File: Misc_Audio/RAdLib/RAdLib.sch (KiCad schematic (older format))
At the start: 18 parts, among them U1 YM3812, U2 YM3014B, U3 RC4136

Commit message: Checkpoint ... board is close to being done.  Still need to tweak the ground plane.
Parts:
- added C1, C2, C3, C4: .1uF, Capacitor_THT:C_Disc_D5.0mm_W2.5mm_P2.50mm, symbol Device:C_Small
- added C5, C56, C6, C61, C7: 10uF, Capacitor_THT:CP_Radial_D5.0mm_P2.50mm, symbol Device:CP1
- added C57: 4.7uF, Capacitor_THT:CP_Radial_D5.0mm_P2.50mm, symbol Device:CP1
- added C58: 1000pF, Capacitor_THT:C_Disc_D5.0mm_W2.5mm_P2.50mm, symbol Device:C
- added C59: 270pF, Capacitor_THT:C_Disc_D5.0mm_W2.5mm_P2.50mm, symbol Device:C
- added C60: .1uF, Capacitor_THT:C_Disc_D5.0mm_W2.5mm_P2.50mm, symbol Device:C
- added C62: .047uF, Capacitor_THT:C_Disc_D5.0mm_W2.5mm_P2.50mm, symbol Device:C
- added C63: 220uF, Capacitor_THT:CP_Axial_L18.0mm_D8.0mm_P25.00mm_Horizontal, symbol Device:CP1
- added D1: 1N4148, Diode_THT:D_DO-35_SOD27_P7.62mm_Horizontal, symbol Device:D
- added J5: AudioJack3, jrt-Connectors:Jack_3.5mm_STX-3120-3B, symbol Connector:AudioJack3
- added Q1: 2N3904, Package_TO_SOT_THT:TO-92_HandSolder, symbol Transistor_BJT:2N3904
- added R10, R12: 2.2K, Resistor_THT:R_Axial_DIN0204_L3.6mm_D1.6mm_P5.08mm_Horizontal, symbol Device:R
- added R11, R15: 10K, Resistor_THT:R_Axial_DIN0204_L3.6mm_D1.6mm_P5.08mm_Horizontal, symbol Device:R
- added R13: 8.2K, Resistor_THT:R_Axial_DIN0204_L3.6mm_D1.6mm_P5.08mm_Horizontal, symbol Device:R
- added R14, R16, R17: 10R, Resistor_THT:R_Axial_DIN0204_L3.6mm_D1.6mm_P5.08mm_Horizontal, symbol Device:R
- added RV1: 10K, jrt-Potentiometers:Potentiometer_Bourns_91A1x_A24, symbol Device:R_POT
- added U4: LM386, Package_DIP:DIP-8_W7.62mm, symbol Amplifier_Audio:LM386
- renumbered C1 to C51, C2 to C52, C3 to C53, C4 to C54, C5 to C55
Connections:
- net FILTER_OUT: now also U3.12, C57.1; no longer U3.3
- net GND: now also C1.2, C2.2, C3.2, C4.2, C5.2, C58.2, C59.2, C6.2, C60.2, C61.2, C7.2, D1.2 (A), J5.S, Q1.1 (E), R11.2, R14.2, R15.2, RV1.3, U4.4 (GND)
- net VCC: now also C1.1, C2.1, C3.1, C4.1, C5.1, C56.1, C6.1, C7.1, U4.6 (V+)
- net at C51.1, U2.7 (RB): now also U3.2 (+); no longer U3.9 (+)
- net at C52.1, R3.1: now also U3.9 (+); no longer U3.2 (+)
- net at C53.1, R4.1, R6.2: now also U3.10; no longer U3.3
- net at R4.2, R5.2: now also U3.8 (-); no longer U3.1 (-)
- net at C54.1, R7.1: now also U3.13 (+); no longer U3.2 (+)
- net at R8.2, R9.2: now also U3.14 (-); no longer U3.1 (-)
- new net: U2.8 (MP), U3.1 (-), U3.3
- new net: C56.2, D1.1 (K), R10.2
- new net: Q1.2 (B), R10.1
- new net: C60.1, U4.2 (-)
- new net: C61.1, U4.7 (BYPASS)
- new net: C62.2, R14.1
- new net AMP_IN: RV1.2, U4.3 (+)
- new net AMP_OUT: C62.1, C63.1, U4.5
- new net AUDIO_OUT: C63.2, R15.1, R16.2, R17.2
- new net LEFT_OUT: J5.T, R16.1
- new net RC1: C57.2, Q1.3 (C), R11.1, R12.2
- new net RC2: C58.1, R12.1, R13.2
- new net RC3: C59.1, R13.1, RV1.1
- new net RIGHT_OUT: J5.R, R17.1
- no-connect marks 0 -> 2
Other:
- note added: "Audio taper"

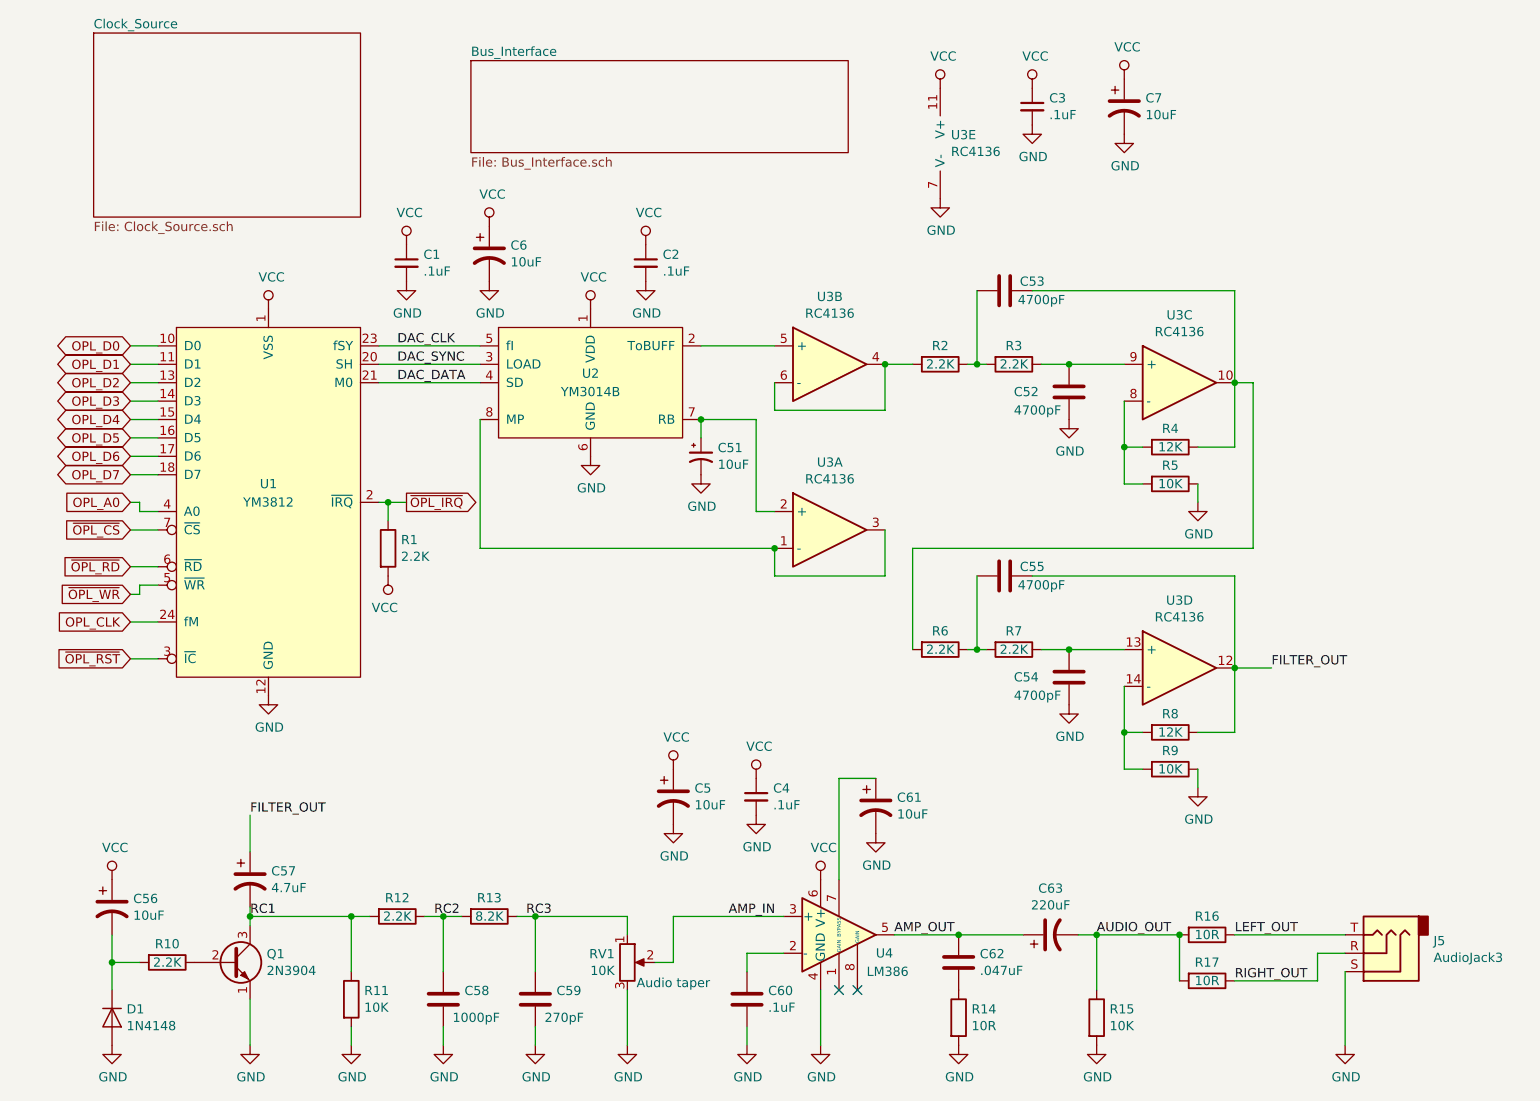
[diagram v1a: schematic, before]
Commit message: Rework the clock to use a self-contained oscillator package.  Remove dependencies on the 7404 in the bus interface.
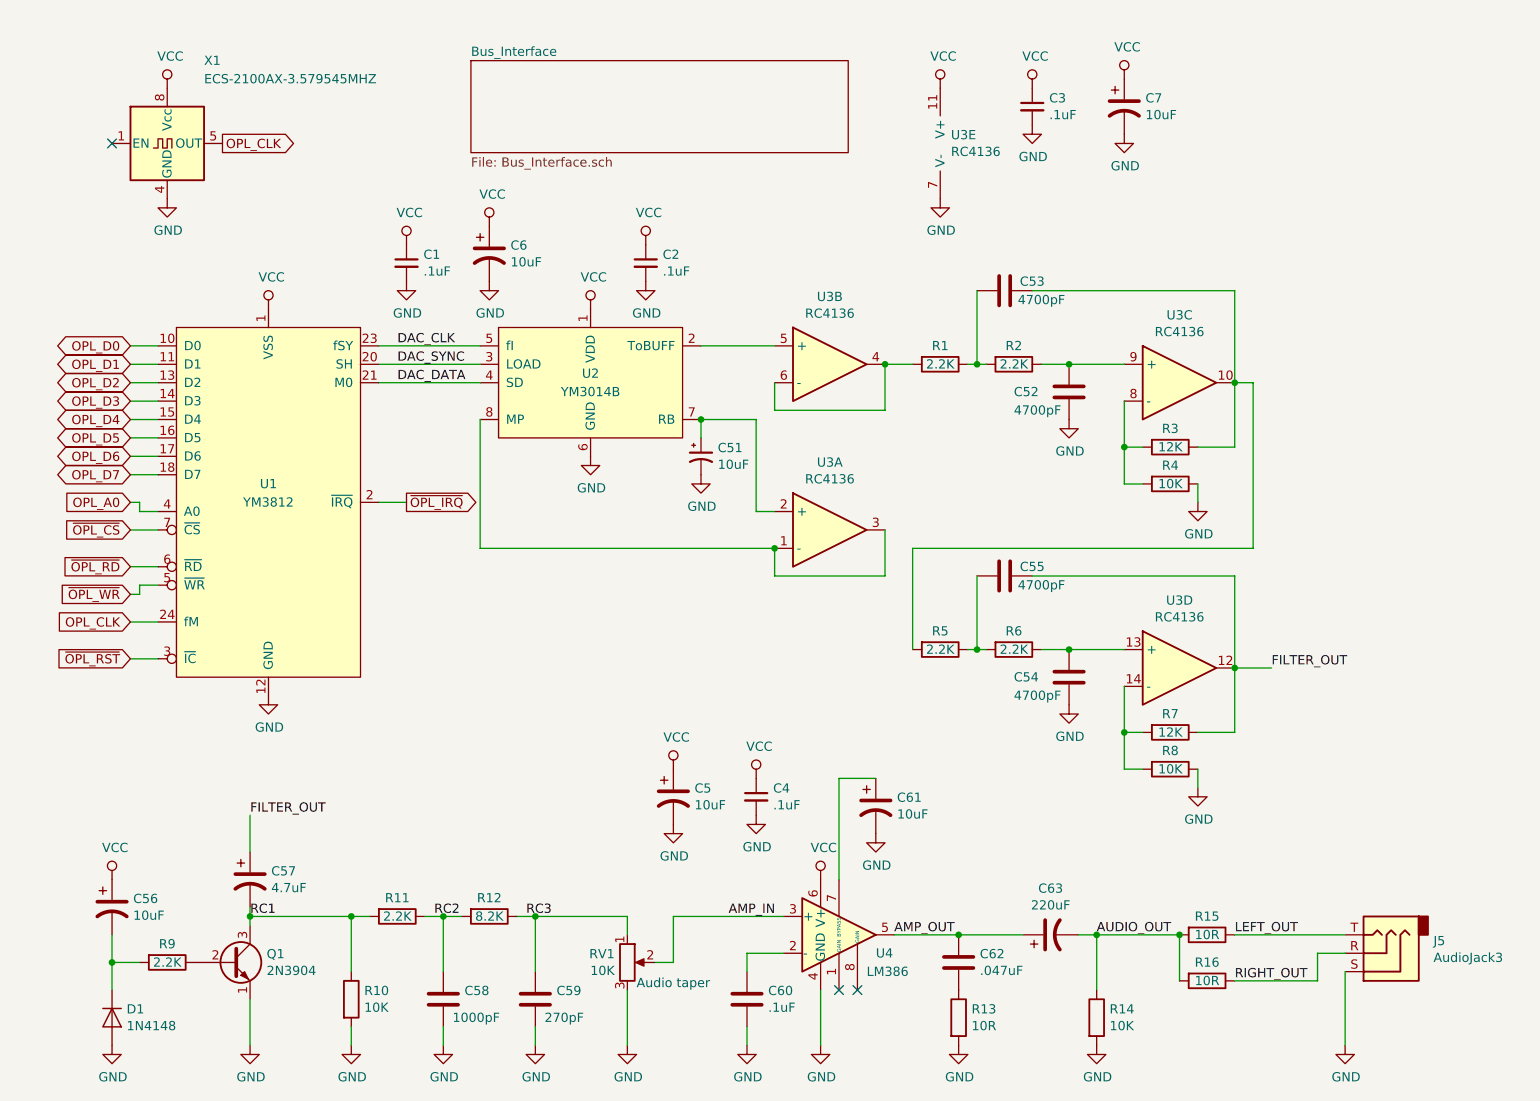
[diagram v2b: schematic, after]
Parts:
- removed R1: 2.2K, Resistor_THT:R_Axial_DIN0204_L3.6mm_D1.6mm_P5.08mm_Horizontal, symbol Device:R
- added X1: ECS-2100AX-3.579545MHZ, Oscillator:Oscillator_DIP-8, symbol Oscillator:CXO_DIP8
- renumbered R2 to R1, R11 to R10, R12 to R11, R13 to R12, R14 to R13, R15 to R14, R16 to R15, R17 to R16, R3 to R2, R4 to R3, R5 to R4, R6 to R5, R7 to R6, R8 to R7, R9 to R8, R10 to R9
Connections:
- net GND: now also X1.4 (GND)
- net OPL_CLK: now also X1.5 (OUT)
- net VCC: now also X1.8 (Vcc)
- no-connect marks 2 -> 3
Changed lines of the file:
@@
 $Descr USLetter 11000 8500
 encoding utf-8
-Sheet 1 3
+Sheet 1 2
 Title "RAdLib - AdLib clone for Raspberry Pi"
 Date "2019-10-10"
@@
 Comment4 ""
 $EndDescr
-$Sheet
-S 800  750  1450 1000
-U 5D9A779A
-F0 "Clock_Source" 50
-F1 "Clock_Source.sch" 50
-$EndSheet
 $Sheet
 S 2850 900  2050 500
@@
 Text GLabel 2500 3300 2    50   Output ~ 0
 ~OPL_IRQ
-Wire Wire Line
-	2350 3300 2400 3300
 $Comp
 L jrt-ICs:RC4136 U3
@@
 $EndComp
 $Comp
-L Device:R R2
+L Device:R R1
 U 1 1 5DAA56E6
 P 5400 2550
-F 0 "R2" V 5300 2550 50  0000 C CNN
+F 0 "R1" V 5300 2550 50  0000 C CNN
 F 1 "2.2K" V 5400 2550 50  0000 C CNN
 F 2 "Resistor_THT:R_Axial_DIN0204_L3.6mm_D1.6mm_P5.08mm_Horizontal" V 5330 2550 50  0001 C CNN
@@
 $EndComp
 $Comp
-L Device:R R3
+L Device:R R2
 U 1 1 5DAA5A5E
 P 5800 2550
-F 0 "R3" V 5700 2550 50  0000 C CNN
+F 0 "R2" V 5700 2550 50  0000 C CNN
 F 1 "2.2K" V 5800 2550 50  0000 C CNN
 F 2 "Resistor_THT:R_Axial_DIN0204_L3.6mm_D1.6mm_P5.08mm_Horizontal" V 5730 2550 50  0001 C CNN
@@
 $EndComp
 $Comp
-L Device:R R4
+L Device:R R3
 U 1 1 5DAA945B
 P 6650 3000
-F 0 "R4" V 6550 3000 50  0000 C CNN
+F 0 "R3" V 6550 3000 50  0000 C CNN
 F 1 "12K" V 6650 3000 50  0000 C CNN
 F 2 "Resistor_THT:R_Axial_DIN0204_L3.6mm_D1.6mm_P5.08mm_Horizontal" V 6580 3000 50  0001 C CNN
@@
 $EndComp
 $Comp
-L Device:R R5
+L Device:R R4
 U 1 1 5DAA9DEE
 P 6650 3200
-F 0 "R5" V 6550 3200 50  0000 C CNN
+F 0 "R4" V 6550 3200 50  0000 C CNN
 F 1 "10K" V 6650 3200 50  0000 C CNN
 F 2 "Resistor_THT:R_Axial_DIN0204_L3.6mm_D1.6mm_P5.08mm_Horizontal" V 6580 3200 50  0001 C CNN
@@
 	5600 2550 5650 2550
 $Comp
-L Device:R R6
+L Device:R R5
 U 1 1 5DABCF38
 P 5400 4100
-F 0 "R6" V 5300 4100 50  0000 C CNN
+F 0 "R5" V 5300 4100 50  0000 C CNN
 F 1 "2.2K" V 5400 4100 50  0000 C CNN
 F 2 "Resistor_THT:R_Axial_DIN0204_L3.6mm_D1.6mm_P5.08mm_Horizontal" V 5330 4100 50  0001 C CNN
@@
 $EndComp
 $Comp
-L Device:R R7
+L Device:R R6
 U 1 1 5DABCF3E
 P 5800 4100
-F 0 "R7" V 5700 4100 50  0000 C CNN
+F 0 "R6" V 5700 4100 50  0000 C CNN
 F 1 "2.2K" V 5800 4100 50  0000 C CNN
 F 2 "Resistor_THT:R_Axial_DIN0204_L3.6mm_D1.6mm_P5.08mm_Horizontal" V 5730 4100 50  0001 C CNN
@@
 $EndComp
 $Comp
-L Device:R R8
+L Device:R R7
 U 1 1 5DABCF56
 P 6650 4550
-F 0 "R8" V 6550 4550 50  0000 C CNN
+F 0 "R7" V 6550 4550 50  0000 C CNN
 F 1 "12K" V 6650 4550 50  0000 C CNN
 F 2 "Resistor_THT:R_Axial_DIN0204_L3.6mm_D1.6mm_P5.08mm_Horizontal" V 6580 4550 50  0001 C CNN
@@
 $EndComp
 $Comp
-L Device:R R9
+L Device:R R8
 U 1 1 5DABCF5C
 P 6650 4750
-F 0 "R9" V 6550 4750 50  0000 C CNN
+F 0 "R8" V 6550 4750 50  0000 C CNN
 F 1 "10K" V 6650 4750 50  0000 C CNN
 F 2 "Resistor_THT:R_Axial_DIN0204_L3.6mm_D1.6mm_P5.08mm_Horizontal" V 6580 4750 50  0001 C CNN
@@
 Wire Wire Line
 	7000 4200 7200 4200
-$Comp
-L Device:R R1
-U 1 1 5DCDFF4A
-P 2400 3550
-F 0 "R1" H 2470 3596 50  0000 L CNN
-F 1 "2.2K" H 2470 3505 50  0000 L CNN
-F 2 "Resistor_THT:R_Axial_DIN0204_L3.6mm_D1.6mm_P5.08mm_Horizontal" V 2330 3550 50  0001 C CNN
-F 3 "~" H 2400 3550 50  0001 C CNN
-	1    2400 3550
-	1    0    0    -1
-$EndComp
-$Comp
-L power:VCC #PWR0112
-U 1 1 5DCE059E
-P 2400 3700
-F 0 "#PWR0112" H 2400 3550 50  0001 C CNN
-F 1 "VCC" H 2418 3873 50  0000 C CNN
-F 2 "" H 2400 3700 50  0001 C CNN
-F 3 "" H 2400 3700 50  0001 C CNN
-	1    2400 3700
-	-1   0    0    1
-$EndComp
-Wire Wire Line
-	2400 3400 2400 3300
-Connection ~ 2400 3300
-Wire Wire Line
-	2400 3300 2500 3300
 $Comp
 L Device:C_Small C?
@@
 $EndComp
 $Comp
-L Device:R R10
+L Device:R R9
 U 1 1 5DAE0710
 P 1200 5800
-F 0 "R10" V 1100 5800 50  0000 C CNN
+F 0 "R9" V 1100 5800 50  0000 C CNN
 F 1 "2.2K" V 1200 5800 50  0000 C CNN
 F 2 "Resistor_THT:R_Axial_DIN0204_L3.6mm_D1.6mm_P5.08mm_Horizontal" V 1130 5800 50  0001 C CNN
@@
 	1650 5500 1650 5550
 $Comp
-L Device:R R11
+L Device:R R10
 U 1 1 5DAEA7A8
 P 2200 6000
-F 0 "R11" H 2270 6046 50  0000 L CNN
+F 0 "R10" H 2270 6046 50  0000 L CNN
 F 1 "10K" H 2270 5955 50  0000 L CNN
 F 2 "Resistor_THT:R_Axial_DIN0204_L3.6mm_D1.6mm_P5.08mm_Horizontal" V 2130 6000 50  0001 C CNN
@@
 	1650 5550 1650 5600
 $Comp
-L Device:R R12
+L Device:R R11
 U 1 1 5DAF0A3B
 P 2450 5550
-F 0 "R12" V 2350 5550 50  0000 C CNN
+F 0 "R11" V 2350 5550 50  0000 C CNN
 F 1 "2.2K" V 2450 5550 50  0000 C CNN
 F 2 "Resistor_THT:R_Axial_DIN0204_L3.6mm_D1.6mm_P5.08mm_Horizontal" V 2380 5550 50  0001 C CNN
@@
 $EndComp
 $Comp
-L Device:R R13
+L Device:R R12
 U 1 1 5DAF0EE4
 P 2950 5550
-F 0 "R13" V 2850 5550 50  0000 C CNN
+F 0 "R12" V 2850 5550 50  0000 C CNN
 F 1 "8.2K" V 2950 5550 50  0000 C CNN
 F 2 "Resistor_THT:R_Axial_DIN0204_L3.6mm_D1.6mm_P5.08mm_Horizontal" V 2880 5550 50  0001 C CNN
@@
 	5150 5650 5500 5650
 $Comp
-L Device:R R14
+L Device:R R13
 U 1 1 5DB38D58
 P 5500 6100
-F 0 "R14" H 5570 6146 50  0000 L CNN
+F 0 "R13" H 5570 6146 50  0000 L CNN
 F 1 "10R" H 5570 6055 50  0000 L CNN
 F 2 "Resistor_THT:R_Axial_DIN0204_L3.6mm_D1.6mm_P5.08mm_Horizontal" V 5430 6100 50  0001 C CNN
@@
 Connection ~ 5500 5650
 $Comp
-L Device:R R15
+L Device:R R14
 U 1 1 5DB3E1C3
 P 6250 6100
-F 0 "R15" H 6320 6146 50  0000 L CNN
+F 0 "R14" H 6320 6146 50  0000 L CNN
 F 1 "10K" H 6320 6055 50  0000 L CNN
 F 2 "Resistor_THT:R_Axial_DIN0204_L3.6mm_D1.6mm_P5.08mm_Horizontal" V 6180 6100 50  0001 C CNN
@@
 AUDIO_OUT
 $Comp
-L Device:R R16
+L Device:R R15
 U 1 1 5DB42AAF
 P 6850 5650
-F 0 "R16" V 6750 5650 50  0000 C CNN
+F 0 "R15" V 6750 5650 50  0000 C CNN
 F 1 "10R" V 6850 5650 50  0000 C CNN
 F 2 "Resistor_THT:R_Axial_DIN0204_L3.6mm_D1.6mm_P5.08mm_Horizontal" V 6780 5650 50  0001 C CNN
@@
 $EndComp
 $Comp
-L Device:R R17
+L Device:R R16
 U 1 1 5DB4338A
 P 6850 5900
-F 0 "R17" V 6750 5900 50  0000 C CNN
+F 0 "R16" V 6750 5900 50  0000 C CNN
 F 1 "10R" V 6850 5900 50  0000 C CNN
 F 2 "Resistor_THT:R_Axial_DIN0204_L3.6mm_D1.6mm_P5.08mm_Horizontal" V 6780 5900 50  0001 C CNN
@@
 	1    0    0    -1
 $EndComp
+$Comp
+L Oscillator:CXO_DIP8 X1
+U 1 1 5DAEC3CE
+P 1200 1350
+F 0 "X1" H 1400 1800 50  0000 L CNN
+F 1 "ECS-2100AX-3.579545MHZ" H 1400 1700 50  0000 L CNN
+F 2 "Oscillator:Oscillator_DIP-8" H 1650 1000 50  0001 C CNN
+F 3 "https://www.mouser.com/datasheet/2/122/ecs-2100x-1084611.pdf" H 1100 1350 50  0001 C CNN
+F 4 "ECS-2100AX-3.579545MHZ" H 1200 1350 50  0001 C CNN "Part"
+	1    1200 1350
+	1    0    0    -1
+$EndComp
+$Comp
+L power:VCC #PWR0113
+U 1 1 5DAEE72D
+P 1200 1050
+F 0 "#PWR0113" H 1200 900 50  0001 C CNN
+F 1 "VCC" H 1217 1223 50  0000 C CNN
+F 2 "" H 1200 1050 50  0001 C CNN
+F 3 "" H 1200 1050 50  0001 C CNN
+	1    1200 1050
+	1    0    0    -1
+$EndComp
+$Comp
+L power:GND #PWR0114
+U 1 1 5DAEF2DF
+P 1200 1650
+F 0 "#PWR0114" H 1200 1400 50  0001 C CNN
+F 1 "GND" H 1205 1477 50  0000 C CNN
+F 2 "" H 1200 1650 50  0001 C CNN
+F 3 "" H 1200 1650 50  0001 C CNN
+	1    1200 1650
+	1    0    0    -1
+$EndComp
+Text GLabel 1500 1350 2    50   Output ~ 0
+OPL_CLK
+NoConn ~ 900  1350
+Wire Wire Line
+	2350 3300 2500 3300
 $EndSCHEMATC

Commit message: Initial rework to simplify the bus interface (removing U202 and U203).
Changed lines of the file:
@@
 	4100 2450 4500 2450
 Wire Wire Line
-	2900 2850 2900 3550
-Wire Wire Line
-	2900 3550 4500 3550
-Wire Wire Line
 	5100 3450 5100 3700
 Wire Wire Line
@@
 Wire Wire Line
 	4500 3700 4500 3550
-Connection ~ 4500 3550
 Wire Wire Line
 	4100 2850 4400 2850
@@
 Wire Wire Line
 	2350 3300 2500 3300
+Wire Wire Line
+	2900 2850 2900 3700
+Wire Wire Line
+	2900 3700 4500 3700
+Connection ~ 4500 3700
 $EndSCHEMATC
